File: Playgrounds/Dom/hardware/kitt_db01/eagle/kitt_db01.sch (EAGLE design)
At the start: 24 parts, among them Q1 [MMBF170], U1 ADNS-3080, U2 MIC5205-3.3YM5TR, X1 RESON

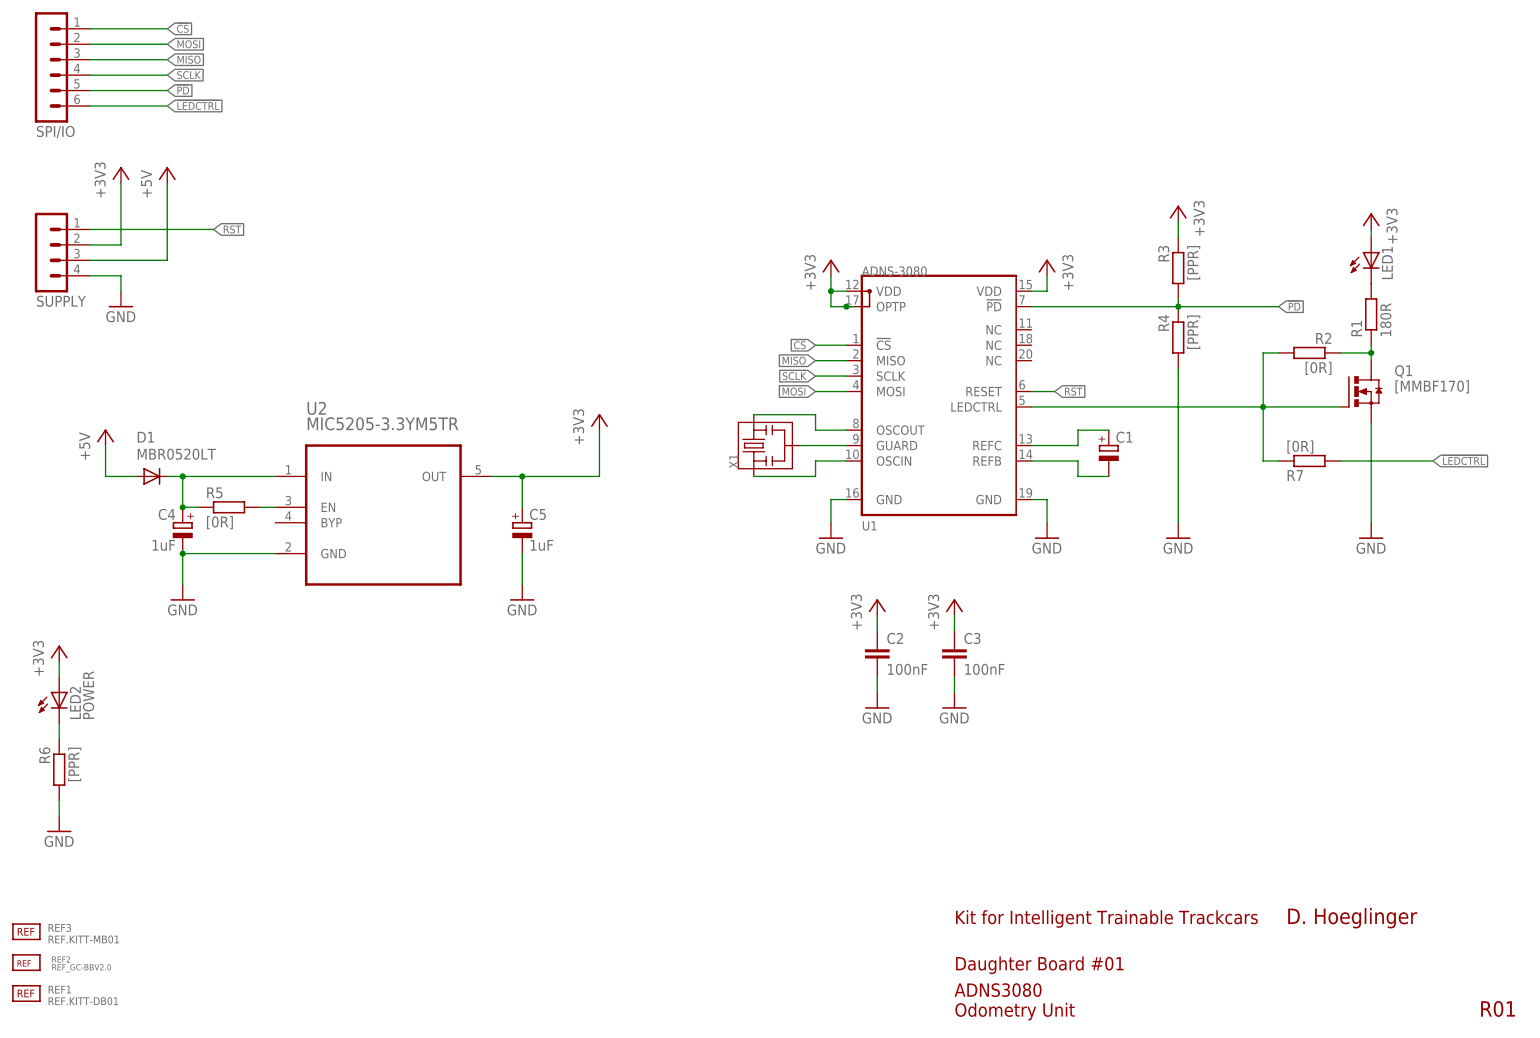
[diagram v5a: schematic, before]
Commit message: placement and basic routing done for db01
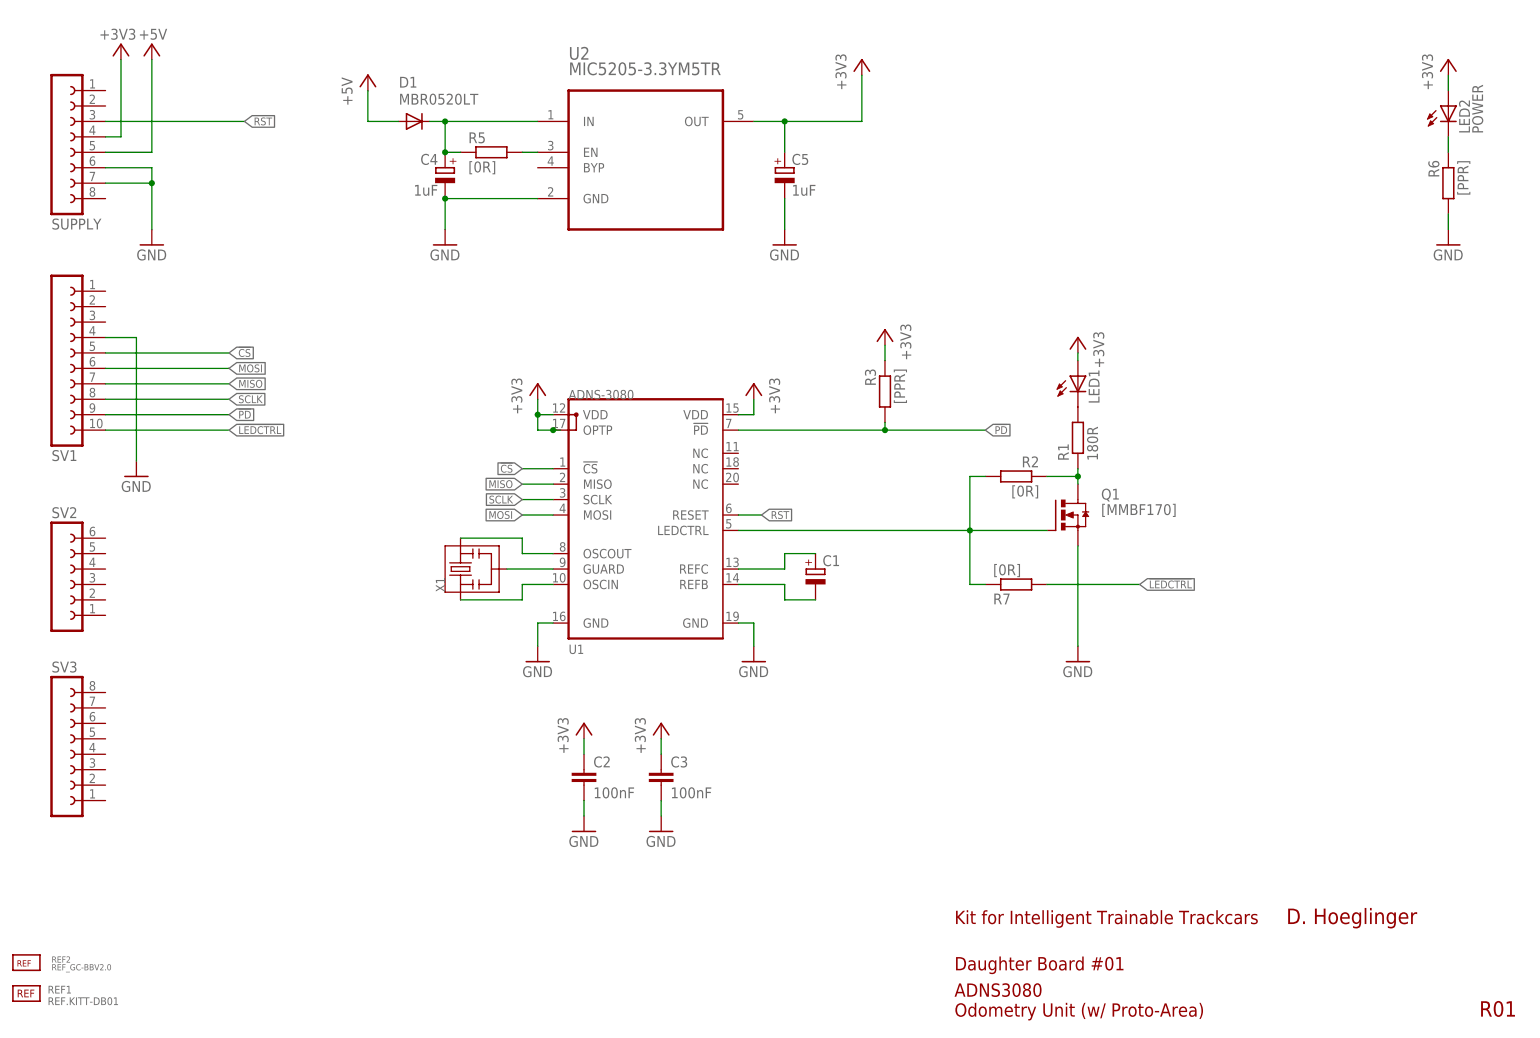
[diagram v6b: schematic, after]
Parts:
- removed R4: [PPR], rcl:R-EU_R0805
- removed REF3: REF.KITT-MB01, kitt.refs:REF.KITT-MB01
- removed SPI/IO: (no value), con-lstb:MA06-1
- added SV1: (no value), con-lsta:FE10-1
- added SV2: (no value), con-lsta:FE06-1
- added SV3: (no value), con-lsta:FE08-1
- SUPPLY: device con-lstb:MA04-1 -> con-lsta:FE08-1
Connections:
- net !CS: now also SV1.5; no longer SPI/IO.1
- net !LEDCTRL: now also SV1.10; no longer SPI/IO.6
- net !PD: now also SV1.9; no longer R4.1, SPI/IO.5
- net +3V3: now also SUPPLY.4; no longer SUPPLY.2
- net +5V: now also SUPPLY.5; no longer SUPPLY.3
- net GND: now also SUPPLY.6, SUPPLY.7, SV1.4; no longer R4.2, SUPPLY.4
- net MISO: now also SV1.7; no longer SPI/IO.3
- net MOSI: now also SV1.6; no longer SPI/IO.2
- net RST: now also SUPPLY.3; no longer SUPPLY.1
- net SCLK: now also SV1.8; no longer SPI/IO.4
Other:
- note added: "ADNS3080 Odometry Unit (w/ Proto-Area)"
- note removed: "ADNS3080 Odometry Unit"
- moved on the sheet: C1, C2, C3, C4, C5, D1, LED1, LED2, Q1, R1, R2, R3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
